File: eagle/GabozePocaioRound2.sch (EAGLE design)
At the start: 32 parts, among them J1 AUDIO_JACK_3.5MM_KIT, J2 SPKR, J3 Batt Conn, J4 ZX62-B-5PA, U1 LM4875

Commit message: Wed  1 May 2019 12:41:43 EDT - changed thermals
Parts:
- A, B: value CONDUCTIVE_BUTTON -> CONDUCTIVE_BUTTONCONDUCTIVE_BUTTON_THICK; device 32teeth - Conductive Buttons:CONDUCTIVE_BUTTON -> 32teeth - Conductive Buttons:CONDUCTIVE_BUTTONCONDUCTIVE_BUTTON_THICK
- DOWN, LEFT, RIGHT, UP: value CONDUCTIVE_BUTTON -> CONDUCTIVE_BUTTONCONDUCTIVE_BUTTON_DIRECTIONAL_THICK; device 32teeth - Conductive Buttons:CONDUCTIVE_BUTTON -> 32teeth - Conductive Buttons:CONDUCTIVE_BUTTONCONDUCTIVE_BUTTON_DIRECTIONAL_THICK
- L1: value CONDUCTIVE_BUTTON_DRILL -> CONDUCTIVE_BUTTON_DRILLCONDUCTIVE_BUTTON_DRILL_THICK; device ConductiveButtons:CONDUCTIVE_BUTTON_DRILL -> 32teeth - Conductive Buttons:CONDUCTIVE_BUTTON_DRILLCONDUCTIVE_BUTTON_DRILL_THICK
- R1, X, Y: value CONDUCTIVE_BUTTON_DRILL -> CONDUCTIVE_BUTTON_DRILLCONDUCTIVE_BUTTON_DRILL_THICK; device 32teeth - Conductive Buttons:CONDUCTIVE_BUTTON_DRILL -> 32teeth - Conductive Buttons:CONDUCTIVE_BUTTON_DRILLCONDUCTIVE_BUTTON_DRILL_THICK
- SELECT, START: value CONDUCTIVE_BUTTON_STARTSELECT -> CONDUCTIVE_BUTTON_STARTSELECTCONDUCTIVE_BUTTON_THICK_STARTSELECT; device 32teeth - Conductive Buttons:CONDUCTIVE_BUTTON_STARTSELECT -> 32teeth - Conductive Buttons:CONDUCTIVE_BUTTON_STARTSELECTCONDUCTIVE_BUTTON_THICK_STARTSELECT

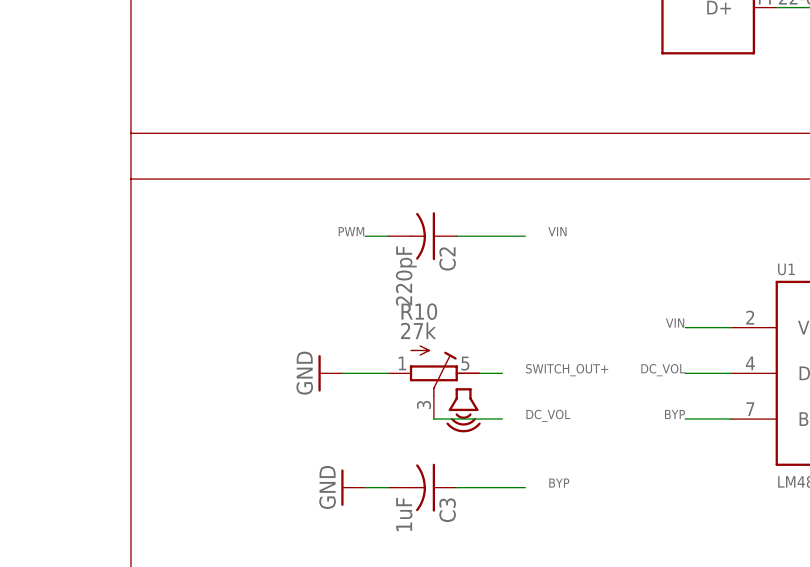
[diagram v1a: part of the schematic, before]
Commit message: Correct the value of C2 to 220nF in Eagle and BOM files
In the datasheet of LM4875 [1], Texas Instruments recommends
a 0.22uF (which is 220nF [2]) AC-coupling capacitor at the
audio input port [3]. However, in the Eagle and BOM files of
Gaboze Pocaio Round 2, the capacitor value was specified
as 220pF by accident. Experiments showed that using a 220pF
capacitor instead of 220nF causes an audible distortion
of the headphone output, which is characterized by the lack
of bass due to the RC high-pass filter action.

This commit corrects the component value C2 from 220pF to
220nF in Eagle schematic and board design files. Also, in
the BOM,

    C2,CAP CER 220PF 50V X7R 0805,C0805C221M5RACTU

has been replaced by

    C2,CAP CER 0.22UF 50V X7R 0805,C0805C224K5RACTU

Applying this fix to the circuit board fixes the audible
distortion and allows the audio quality to be restored
to TI's reference design.

It should be note that the Gerber files are not corrected,
since the committer doesn't have the project settings required
to create an identical set of Gerber files. The Gerber files
should be updated in a later commit by the original author.

[1] https://www.ti.com/lit/ds/symlink/lm4875.pdf

[2] https://en.wikipedia.org/wiki/Metric_prefix

[3] See Figure 1.

Signed-off-by: Tom Li <tomli@tomli.me>
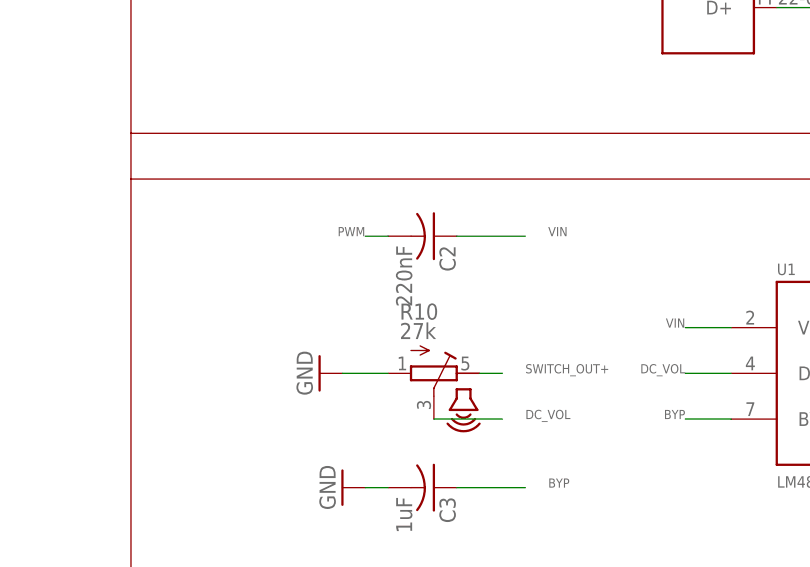
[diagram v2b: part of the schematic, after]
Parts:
- C2: value 220pF -> 220nF
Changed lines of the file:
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@@
 <part name="U$1" library="SparkFun-Retired" library_urn="urn:adsk.eagle:library:533" deviceset="SWITCH_SPDT" device=""/>
 <part name="U1" library="texas" library_urn="urn:adsk.eagle:library:387" deviceset="LM4875" device=""/>
-<part name="C2" library="adafruit" library_urn="urn:adsk.eagle:library:420" deviceset="C-US" device="C0805" value="220pF"/>
+<part name="C2" library="adafruit" library_urn="urn:adsk.eagle:library:420" deviceset="C-US" device="C0805" value="220nF"/>
 <part name="GND29" library="SparkFun-Aesthetics" library_urn="urn:adsk.eagle:library:507" deviceset="GND" device=""/>
 <part name="C3" library="adafruit" library_urn="urn:adsk.eagle:library:420" deviceset="C-US" device="C0805" value="1uF"/>
